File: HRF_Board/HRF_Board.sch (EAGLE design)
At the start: 14 parts, among them U1 MAX30101EFD

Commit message: Things and stuff
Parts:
- removed R4, R5: 4.7k, SparkFun-Resistors:100KOHM-0603-1/10W-1%
- added U$9: FLAT_FLEX_8, FLAT_FLEX:FLAT_FLEX_8
- added Y1: ABS06-107-32.768KHZ-T, ABS06-107-32.768KHZ-T:ABS06-107-32.768KHZ-T
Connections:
- removed net N$2: C2.1, U$1.VDD@2
- new net N$1: U$1.32KIN, Y1.2
- new net N$3: U$1.32KOUT, Y1.1
- net 1.8V: now also C2.1, U$1.VDD@2, U$9.4; no longer R4.2, R5.2
- net 3.3V: now also U$9.3
- net GND: now also U$9.1
- net MFIO: now also U$9.7
- net RSTN: now also U$9.8
- net SCL_WMD: now also U$9.6; no longer R5.1
- net SDA_WMD: now also U$9.5; no longer R4.1
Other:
- note added: "PUT PULL UP RESISTORS FOR I2C ON WMD BOARD!!"
- moved on the sheet: C2

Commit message: Fully routed
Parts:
- removed C2, C3, C4: 1uF, SparkFun-Capacitors:1.0UF-0603-16V-10%
- removed C5: 100nF, SparkFun-Capacitors:1.0UF-0603-16V-10%
- removed R6: 10, SparkFun-Resistors:100KOHM-0603-1/10W-1%
- removed U$1: MAX32664_TQFN, MAX32664:MAX32664_TQFN
- removed Y1: ABS06-107-32.768KHZ-T, ABS06-107-32.768KHZ-T:ABS06-107-32.768KHZ-T
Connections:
- removed net MFIO: U$1.MFIO, U$9.7
- removed net N$1: U$1.32KIN, Y1.2
- removed net N$3: U$1.32KOUT, Y1.1
- removed net N$4: C4.2, U$1.VCORE
- removed net N$7: C5.2, R6.2
- removed net RSTN: C5.1, U$1.RSTN, U$9.8
- removed net SCL_WMD: U$1.SLAVE_SCL, U$9.6
- removed net SDA_WMD: U$1.SLAVE_SDA, U$9.5
- net 1.8V: now also U$9.8; no longer C2.1, C3.1, U$1.VDD@1, U$1.VDD@2, U$9.4
- net 3.3V: now also U$9.6; no longer U$9.3
- net GND: now also U$9.2; no longer C2.2, C3.2, C4.1, R6.1, U$1.EP, U$1.VSS@1, U$1.VSS@2
- net HR_SCL: now also U$9.4; no longer U$1.SENSOR_SCL
- net HR_SDA: now also U$9.5; no longer U$1.SENSOR_SDA
- net INT: now also U$9.7; no longer U$1.HR_INT
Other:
- note removed: "PUT PULL UP RESISTORS FOR I2C ON WMD BOARD!!"

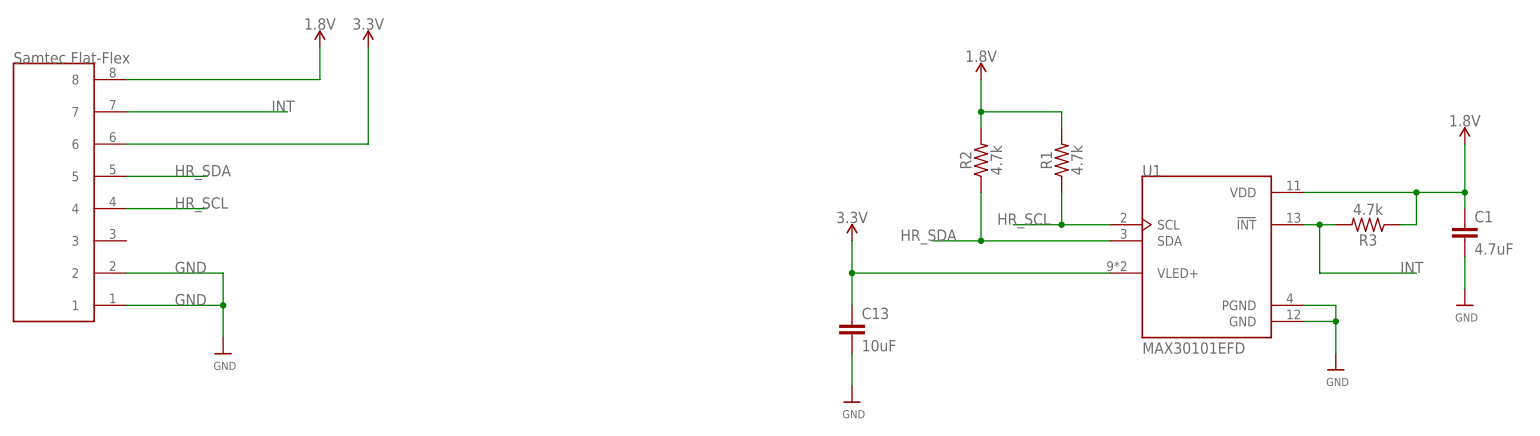
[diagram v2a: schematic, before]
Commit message: Rerouted with new connector and added full ground plane
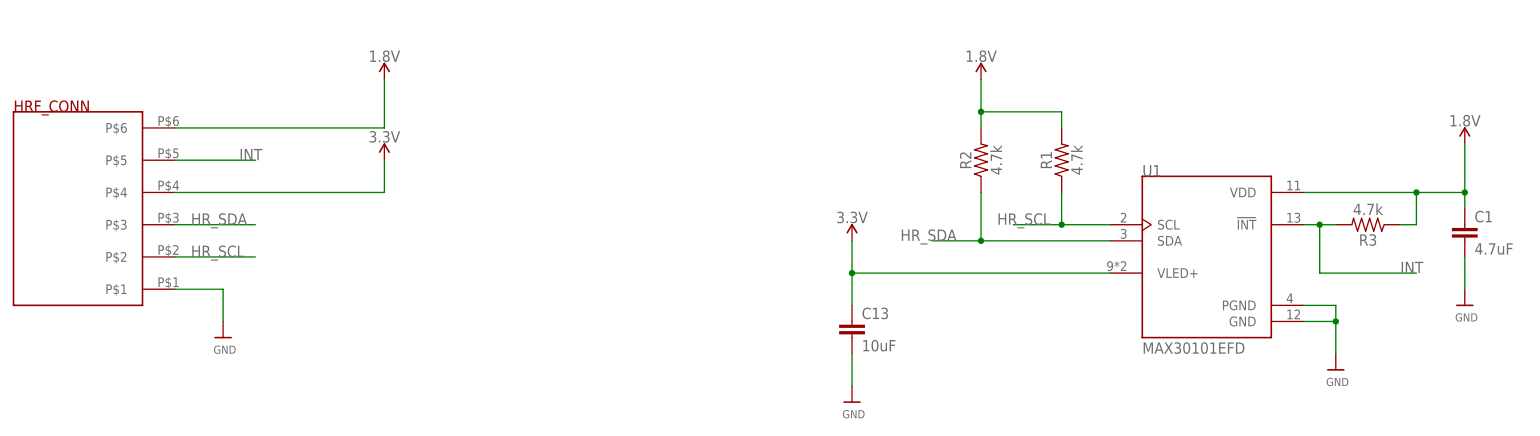
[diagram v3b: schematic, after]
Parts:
- removed U$9: FLAT_FLEX_8, FLAT_FLEX:FLAT_FLEX_8
- added U$1: HRF_CONN, HRF_CONN:HRF_CONN
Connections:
- net 1.8V: now also U$1.P$6; no longer U$9.8
- net 3.3V: now also U$1.P$4; no longer U$9.6
- net GND: now also U$1.P$1; no longer U$9.1, U$9.2
- net HR_SCL: now also U$1.P$2; no longer U$9.4
- net HR_SDA: now also U$1.P$3; no longer U$9.5
- net INT: now also U$1.P$5; no longer U$9.7
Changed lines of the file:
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@@
 <?xml version="1.0" encoding="utf-8"?>
 <!DOCTYPE eagle SYSTEM "eagle.dtd">
-<eagle version="8.6.1">
+<eagle version="9.5.2">
 <drawing>
 <settings>
@@
 <part name="SUPPLY2" library="SparkFun-PowerSymbols" library_urn="urn:adsk.eagle:library:530" deviceset="1.8V" device=""/>
 <part name="R3" library="SparkFun-Resistors" library_urn="urn:adsk.eagle:library:532" deviceset="100KOHM" device="-0603-1/10W-1%" package3d_urn="urn:adsk.eagle:package:39650/1" value="4.7k"/>
-<part name="U$9" library="FLAT_FLEX" deviceset="FLAT_FLEX_8" device=""/>
-<part name="U$10" library="microbuilder" deviceset="GND" device=""/>
-<part name="SUPPLY5" library="SparkFun-PowerSymbols" library_urn="urn:adsk.eagle:library:530" deviceset="1.8V" device=""/>
-<part name="SUPPLY6" library="SparkFun-PowerSymbols" library_urn="urn:adsk.eagle:library:530" deviceset="3.3V" device=""/>
+<part name="U$1" library="HRF_CONN" deviceset="HRF_CONN" device=""/>
+<part name="U$4" library="microbuilder" deviceset="GND" device=""/>
+<part name="SUPPLY3" library="SparkFun-PowerSymbols" library_urn="urn:adsk.eagle:library:530" deviceset="3.3V" device=""/>
+<part name="SUPPLY4" library="SparkFun-PowerSymbols" library_urn="urn:adsk.eagle:library:530" deviceset="1.8V" device=""/>
 </parts>
 <sheets>
@@
 </plain>
 <instances>
-<instance part="FRAME1" gate="G$1" x="0" y="0"/>
-<instance part="U1" gate="G$1" x="259.08" y="205.74"/>
-<instance part="R1" gate="G$1" x="236.22" y="220.98" rot="R90"/>
-<instance part="R2" gate="G$1" x="223.52" y="220.98" rot="R90"/>
-<instance part="SUPPLY1" gate="G$1" x="223.52" y="233.68"/>
-<instance part="C13" gate="G$1" x="203.2" y="193.04"/>
-<instance part="U$14" gate="G$1" x="203.2" y="182.88"/>
-<instance part="SUPPLY14" gate="G$1" x="203.2" y="208.28"/>
-<instance part="U$2" gate="G$1" x="279.4" y="187.96"/>
-<instance part="C1" gate="G$1" x="299.72" y="208.28"/>
-<instance part="U$3" gate="G$1" x="299.72" y="198.12"/>
-<instance part="SUPPLY2" gate="G$1" x="299.72" y="223.52"/>
-<instance part="R3" gate="G$1" x="284.48" y="210.82" rot="R180"/>
-<instance part="U$9" gate="G$1" x="71.12" y="195.58"/>
-<instance part="U$10" gate="G$1" x="104.14" y="190.5"/>
-<instance part="SUPPLY5" gate="G$1" x="119.38" y="238.76"/>
-<instance part="SUPPLY6" gate="G$1" x="127" y="238.76"/>
+<instance part="FRAME1" gate="G$1" x="0" y="0" smashed="yes">
+<attribute name="DRAWING_NAME" x="344.17" y="15.24" size="2.54" layer="94"/>
+<attribute name="LAST_DATE_TIME" x="344.17" y="10.16" size="2.286" layer="94"/>
+<attribute name="SHEET" x="357.505" y="5.08" size="2.54" layer="94"/>
+</instance>
+<instance part="U1" gate="G$1" x="259.08" y="205.74" smashed="yes">
+<attribute name="NAME" x="248.92" y="218.44" size="1.778" layer="95"/>
+<attribute name="VALUE" x="248.92" y="190.5" size="1.778" layer="96"/>
+</instance>
+<instance part="R1" gate="G$1" x="236.22" y="220.98" smashed="yes" rot="R90">
+<attribute name="NAME" x="234.696" y="220.98" size="1.778" layer="95" font="vector" rot="R90" align="bottom-center"/>
+<attribute name="VALUE" x="237.744" y="220.98" size="1.778" layer="96" font="vector" rot="R90" align="top-center"/>
+</instance>
+<instance part="R2" gate="G$1" x="223.52" y="220.98" smashed="yes" rot="R90">
+<attribute name="NAME" x="221.996" y="220.98" size="1.778" layer="95" font="vector" rot="R90" align="bottom-center"/>
+<attribute name="VALUE" x="225.044" y="220.98" size="1.778" layer="96" font="vector" rot="R90" align="top-center"/>
+</instance>
+<instance part="SUPPLY1" gate="G$1" x="223.52" y="233.68" smashed="yes">
+<attribute name="VALUE" x="223.52" y="236.474" size="1.778" layer="96" align="bottom-center"/>
+</instance>
+<instance part="C13" gate="G$1" x="203.2" y="193.04" smashed="yes">
+<attribute name="NAME" x="204.724" y="195.961" size="1.778" layer="95" font="vector"/>
+<attribute name="VALUE" x="204.724" y="190.881" size="1.778" layer="96" font="vector"/>
+</instance>
+<instance part="U$14" gate="G$1" x="203.2" y="182.88" smashed="yes">
+<attribute name="VALUE" x="201.676" y="180.34" size="1.27" layer="96"/>
+</instance>
+<instance part="SUPPLY14" gate="G$1" x="203.2" y="208.28" smashed="yes">
+<attribute name="VALUE" x="203.2" y="211.074" size="1.778" layer="96" align="bottom-center"/>
+</instance>
+<instance part="U$2" gate="G$1" x="279.4" y="187.96" smashed="yes">
+<attribute name="VALUE" x="277.876" y="185.42" size="1.27" layer="96"/>
+</instance>
+<instance part="C1" gate="G$1" x="299.72" y="208.28" smashed="yes">
+<attribute name="NAME" x="301.244" y="211.201" size="1.778" layer="95" font="vector"/>
+<attribute name="VALUE" x="301.244" y="206.121" size="1.778" layer="96" font="vector"/>
+</instance>
+<instance part="U$3" gate="G$1" x="299.72" y="198.12" smashed="yes">
+<attribute name="VALUE" x="298.196" y="195.58" size="1.27" layer="96"/>
+</instance>
+<instance part="SUPPLY2" gate="G$1" x="299.72" y="223.52" smashed="yes">
+<attribute name="VALUE" x="299.72" y="226.314" size="1.778" layer="96" align="bottom-center"/>
+</instance>
+<instance part="R3" gate="G$1" x="284.48" y="210.82" smashed="yes" rot="R180">
+<attribute name="NAME" x="284.48" y="209.296" size="1.778" layer="95" font="vector" rot="R180" align="bottom-center"/>
+<attribute name="VALUE" x="284.48" y="212.344" size="1.778" layer="96" font="vector" rot="R180" align="top-center"/>
+</instance>
+<instance part="U$1" gate="G$1" x="71.12" y="198.12" smashed="yes"/>
+<instance part="U$4" gate="G$1" x="104.14" y="193.04" smashed="yes">
+<attribute name="VALUE" x="102.616" y="190.5" size="1.27" layer="96"/>
+</instance>
+<instance part="SUPPLY3" gate="G$1" x="129.54" y="220.98" smashed="yes">
+<attribute name="VALUE" x="129.54" y="223.774" size="1.778" layer="96" align="bottom-center"/>
+</instance>
+<instance part="SUPPLY4" gate="G$1" x="129.54" y="233.68" smashed="yes">
+<attribute name="VALUE" x="129.54" y="236.474" size="1.778" layer="96" align="bottom-center"/>
+</instance>
 </instances>
 <busses>
@@
 </segment>
 <segment>
-<pinref part="U$9" gate="G$1" pin="5"/>
-<wire x1="88.9" y1="218.44" x2="101.6" y2="218.44" width="0.1524" layer="91"/>
-<label x="96.52" y="218.44" size="1.778" layer="95"/>
+<pinref part="U$1" gate="G$1" pin="P$3"/>
+<wire x1="96.52" y1="210.82" x2="109.22" y2="210.82" width="0.1524" layer="91"/>
+<label x="99.06" y="210.82" size="1.778" layer="95"/>
 </segment>
 </net>
@@
 </segment>
 <segment>
-<pinref part="U$9" gate="G$1" pin="4"/>
-<wire x1="88.9" y1="213.36" x2="101.6" y2="213.36" width="0.1524" layer="91"/>
-<label x="96.52" y="213.36" size="1.778" layer="95"/>
+<pinref part="U$1" gate="G$1" pin="P$2"/>
+<wire x1="96.52" y1="205.74" x2="109.22" y2="205.74" width="0.1524" layer="91"/>
+<label x="99.06" y="205.74" size="1.778" layer="95"/>
 </segment>
 </net>
@@
 </segment>
 <segment>
-<pinref part="U$9" gate="G$1" pin="8"/>
-<pinref part="SUPPLY5" gate="G$1" pin="1.8V"/>
-<wire x1="88.9" y1="233.68" x2="119.38" y2="233.68" width="0.1524" layer="91"/>
-<wire x1="119.38" y1="233.68" x2="119.38" y2="238.76" width="0.1524" layer="91"/>
+<pinref part="U$1" gate="G$1" pin="P$6"/>
+<pinref part="SUPPLY4" gate="G$1" pin="1.8V"/>
+<wire x1="96.52" y1="226.06" x2="129.54" y2="226.06" width="0.1524" layer="91"/>
+<wire x1="129.54" y1="226.06" x2="129.54" y2="233.68" width="0.1524" layer="91"/>
 </segment>
 </net>
@@
 </segment>
 <segment>
-<pinref part="SUPPLY6" gate="G$1" pin="3.3V"/>
-<wire x1="127" y1="223.52" x2="127" y2="238.76" width="0.1524" layer="91"/>
-<pinref part="U$9" gate="G$1" pin="6"/>
-<wire x1="88.9" y1="223.52" x2="127" y2="223.52" width="0.1524" layer="91"/>
+<pinref part="U$1" gate="G$1" pin="P$4"/>
+<pinref part="SUPPLY3" gate="G$1" pin="3.3V"/>
+<wire x1="96.52" y1="215.9" x2="129.54" y2="215.9" width="0.1524" layer="91"/>
+<wire x1="129.54" y1="215.9" x2="129.54" y2="220.98" width="0.1524" layer="91"/>
 </segment>
 </net>
@@
 </segment>
 <segment>
-<pinref part="U$9" gate="G$1" pin="2"/>
-<wire x1="88.9" y1="203.2" x2="104.14" y2="203.2" width="0.1524" layer="91"/>
-<label x="96.52" y="203.2" size="1.778" layer="95"/>
-<pinref part="U$10" gate="G$1" pin="GND"/>
-<wire x1="104.14" y1="203.2" x2="104.14" y2="198.12" width="0.1524" layer="91"/>
-<pinref part="U$9" gate="G$1" pin="1"/>
-<wire x1="104.14" y1="198.12" x2="104.14" y2="193.04" width="0.1524" layer="91"/>
-<wire x1="88.9" y1="198.12" x2="104.14" y2="198.12" width="0.1524" layer="91"/>
-<label x="96.52" y="198.12" size="1.778" layer="95"/>
-<junction x="104.14" y="198.12"/>
+<pinref part="U$1" gate="G$1" pin="P$1"/>
+<pinref part="U$4" gate="G$1" pin="GND"/>
+<wire x1="96.52" y1="200.66" x2="104.14" y2="200.66" width="0.1524" layer="91"/>
+<wire x1="104.14" y1="200.66" x2="104.14" y2="195.58" width="0.1524" layer="91"/>
 </segment>
 </net>
@@
 </segment>
 <segment>
-<pinref part="U$9" gate="G$1" pin="7"/>
-<wire x1="88.9" y1="228.6" x2="114.3" y2="228.6" width="0.1524" layer="91"/>
-<label x="111.76" y="228.6" size="1.778" layer="95"/>
-</segment>
-</net>
+<pinref part="U$1" gate="G$1" pin="P$5"/>
+<wire x1="96.52" y1="220.98" x2="109.22" y2="220.98" width="0.1524" layer="91"/>
+<label x="106.68" y="220.98" size="1.778" layer="95"/>
+</segment>
+</net>
